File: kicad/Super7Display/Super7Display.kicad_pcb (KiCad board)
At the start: 2 copper layers, 180.3 x 33 mm, 8 parts, among them P1 CONN_01X13, P2 CONN_01X09

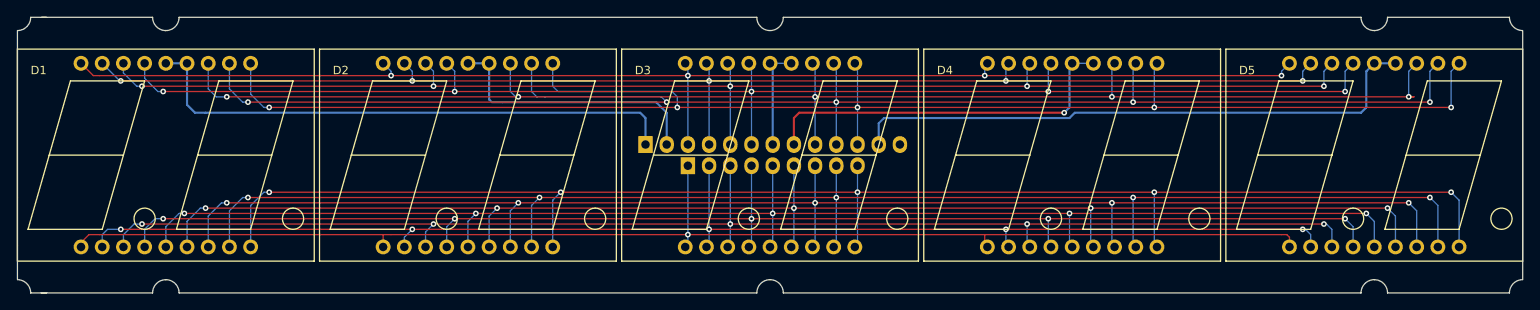
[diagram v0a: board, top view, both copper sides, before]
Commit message: Make display's board outline the same size as the digits
Only saves $5.30 on OSH Park
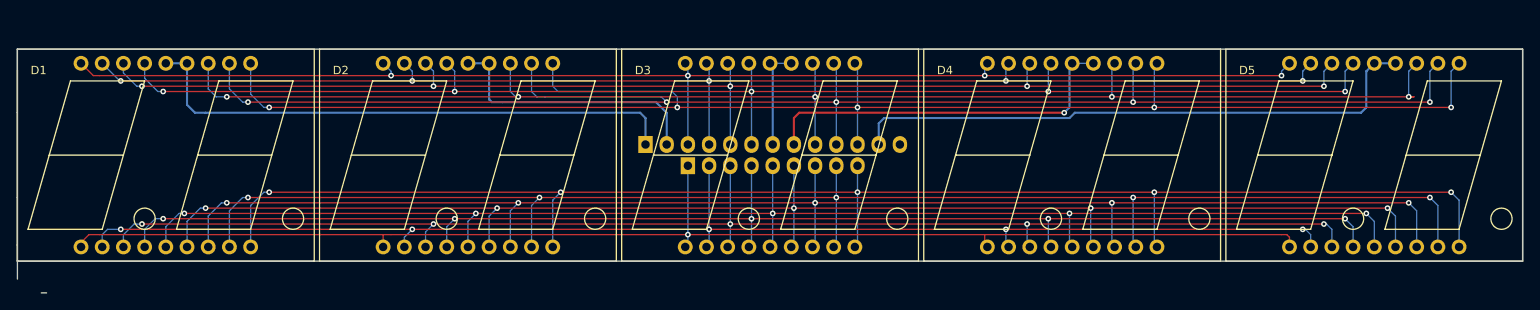
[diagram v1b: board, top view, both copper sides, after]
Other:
- board size 180.3 x 33 mm -> 180.3 x 29.2 mm
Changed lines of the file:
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@@
     (area 163.548287 45.814 356.779901 83.895001)
     (thickness 1.6)
-    (drawings 39)
+    (drawings 16)
     (tracks 343)
     (zones 0)
@@
     (44 Edge.Cuts user)
     (45 Margin user)
-    (46 B.CrtYd user hide)
-    (47 F.CrtYd user hide)
+    (46 B.CrtYd user)
+    (47 F.CrtYd user)
     (48 B.Fab user)
     (49 F.Fab user)
@@
     )
   )
-  (gr_line (start 195.58 83.82) (end 264.795 83.82) (angle 90) (layer Edge.Cuts) (width 0.15))
-  (gr_line (start 337.185 83.82) (end 267.97 83.82) (angle 90) (layer Edge.Cuts) (width 0.15))
-  (gr_line (start 354.965 83.82) (end 340.36 83.82) (angle 90) (layer Edge.Cuts) (width 0.15))
-  (gr_line (start 340.36 50.8) (end 354.965 50.8) (angle 90) (layer Edge.Cuts) (width 0.15))
-  (gr_line (start 267.97 50.8) (end 337.185 50.8) (angle 90) (layer Edge.Cuts) (width 0.15))
-  (gr_line (start 195.58 50.8) (end 264.795 50.8) (angle 90) (layer Edge.Cuts) (width 0.15))
+  (gr_line (start 356.5398 80.01) (end 356.5398 54.61) (angle 90) (layer Edge.Cuts) (width 0.15))
+  (gr_line (start 176.1998 80.01) (end 176.276 80.01) (angle 90) (layer Edge.Cuts) (width 0.15))
+  (gr_line (start 176.1998 54.61) (end 176.1998 80.01) (angle 90) (layer Edge.Cuts) (width 0.15))
+  (gr_line (start 176.1998 54.61) (end 176.1998 54.5846) (angle 90) (layer Edge.Cuts) (width 0.15))
+  (gr_line (start 356.5398 54.61) (end 176.1998 54.61) (angle 90) (layer Edge.Cuts) (width 0.15))
+  (gr_line (start 176.2252 80.01) (end 356.5398 80.01) (angle 90) (layer Edge.Cuts) (width 0.15))
   (dimension 180.34 (width 0.3) (layer F.Fab)
     (gr_text "7.1000 in" (at 266.319 47.164) (layer F.Fab)
@@
     (arrow2b (pts (xy 172.974 50.8) (xy 173.560421 51.926504)))
   )
-  (gr_line (start 179.07 50.8) (end 179.705 50.8) (angle 90) (layer Edge.Cuts) (width 0.15))
   (gr_line (start 179.07 83.82) (end 179.705 83.82) (angle 90) (layer Edge.Cuts) (width 0.15))
-  (gr_line (start 177.8 83.82) (end 179.3875 83.82) (angle 90) (layer Edge.Cuts) (width 0.15))
-  (gr_line (start 177.8 50.8) (end 179.3875 50.8) (angle 90) (layer Edge.Cuts) (width 0.15))
-  (gr_line (start 356.5525 82.169) (end 356.5525 52.451) (angle 90) (layer Edge.Cuts) (width 0.15))
-  (gr_arc (start 356.5525 83.82) (end 354.965 83.82) (angle 90) (layer Edge.Cuts) (width 0.15))
-  (gr_arc (start 356.5525 50.8) (end 356.5525 52.3875) (angle 90) (layer Edge.Cuts) (width 0.15))
-  (gr_line (start 179.451 83.82) (end 192.405 83.82) (angle 90) (layer Edge.Cuts) (width 0.15))
-  (gr_line (start 179.451 50.8) (end 192.405 50.8) (angle 90) (layer Edge.Cuts) (width 0.15))
-  (gr_line (start 176.2125 52.451) (end 176.2125 57.15) (angle 90) (layer Edge.Cuts) (width 0.15))
   (gr_line (start 176.2125 82.169) (end 176.2125 78.105) (angle 90) (layer Edge.Cuts) (width 0.15))
-  (gr_arc (start 176.2125 83.82) (end 176.2125 82.2325) (angle 90) (layer Edge.Cuts) (width 0.15))
-  (gr_arc (start 176.2125 50.8) (end 177.8 50.8) (angle 90) (layer Edge.Cuts) (width 0.15))
-  (gr_arc (start 266.3825 50.8) (end 266.3825 52.3875) (angle 90) (layer Edge.Cuts) (width 0.15))
-  (gr_arc (start 338.7725 50.8) (end 338.7725 52.3875) (angle 90) (layer Edge.Cuts) (width 0.15))
-  (gr_arc (start 338.7725 50.8) (end 340.36 50.8) (angle 90) (layer Edge.Cuts) (width 0.15))
-  (gr_arc (start 338.7725 83.82) (end 337.185 83.82) (angle 90) (layer Edge.Cuts) (width 0.15))
-  (gr_arc (start 338.7725 83.82) (end 338.7725 82.2325) (angle 90) (layer Edge.Cuts) (width 0.15))
-  (gr_arc (start 193.9925 83.82) (end 193.9925 82.2325) (angle 90) (layer Edge.Cuts) (width 0.15))
-  (gr_arc (start 193.9925 83.82) (end 192.405 83.82) (angle 90) (layer Edge.Cuts) (width 0.15))
-  (gr_arc (start 193.9925 50.8) (end 195.58 50.8) (angle 90) (layer Edge.Cuts) (width 0.15))
-  (gr_arc (start 193.9925 50.8) (end 193.9925 52.3875) (angle 90) (layer Edge.Cuts) (width 0.15))
   (gr_line (start 176.2125 62.23) (end 176.2125 57.15) (angle 90) (layer Edge.Cuts) (width 0.15))
   (gr_line (start 176.2125 72.39) (end 176.2125 78.105) (angle 90) (layer Edge.Cuts) (width 0.15))
@@
     (effects (font (size 1.5 1.5) (thickness 0.2)) (justify mirror))
   )
-  (gr_arc (start 266.3825 83.82) (end 264.795 83.82) (angle 90) (layer Edge.Cuts) (width 0.15))
-  (gr_arc (start 266.3825 83.82) (end 266.3825 82.2325) (angle 90) (layer Edge.Cuts) (width 0.15))
-  (gr_arc (start 266.3825 50.8) (end 267.97 50.8) (angle 90) (layer Edge.Cuts) (width 0.15))
   (gr_line (start 176.2125 62.23) (end 176.2125 72.39) (angle 90) (layer Edge.Cuts) (width 0.15))
   (segment (start 186.055 76.835) (end 184.785 76.835) (width 0.1524) (layer F.Cu) (net 1))
